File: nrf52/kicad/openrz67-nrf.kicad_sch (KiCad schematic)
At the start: 14 parts, among them J1 Camera, J2 SWD, Q1 AO3401A, SW1 B3U-1000P, U1 E73-2G4M08S1F, U2 TLP172AM, U3 TLP172AM

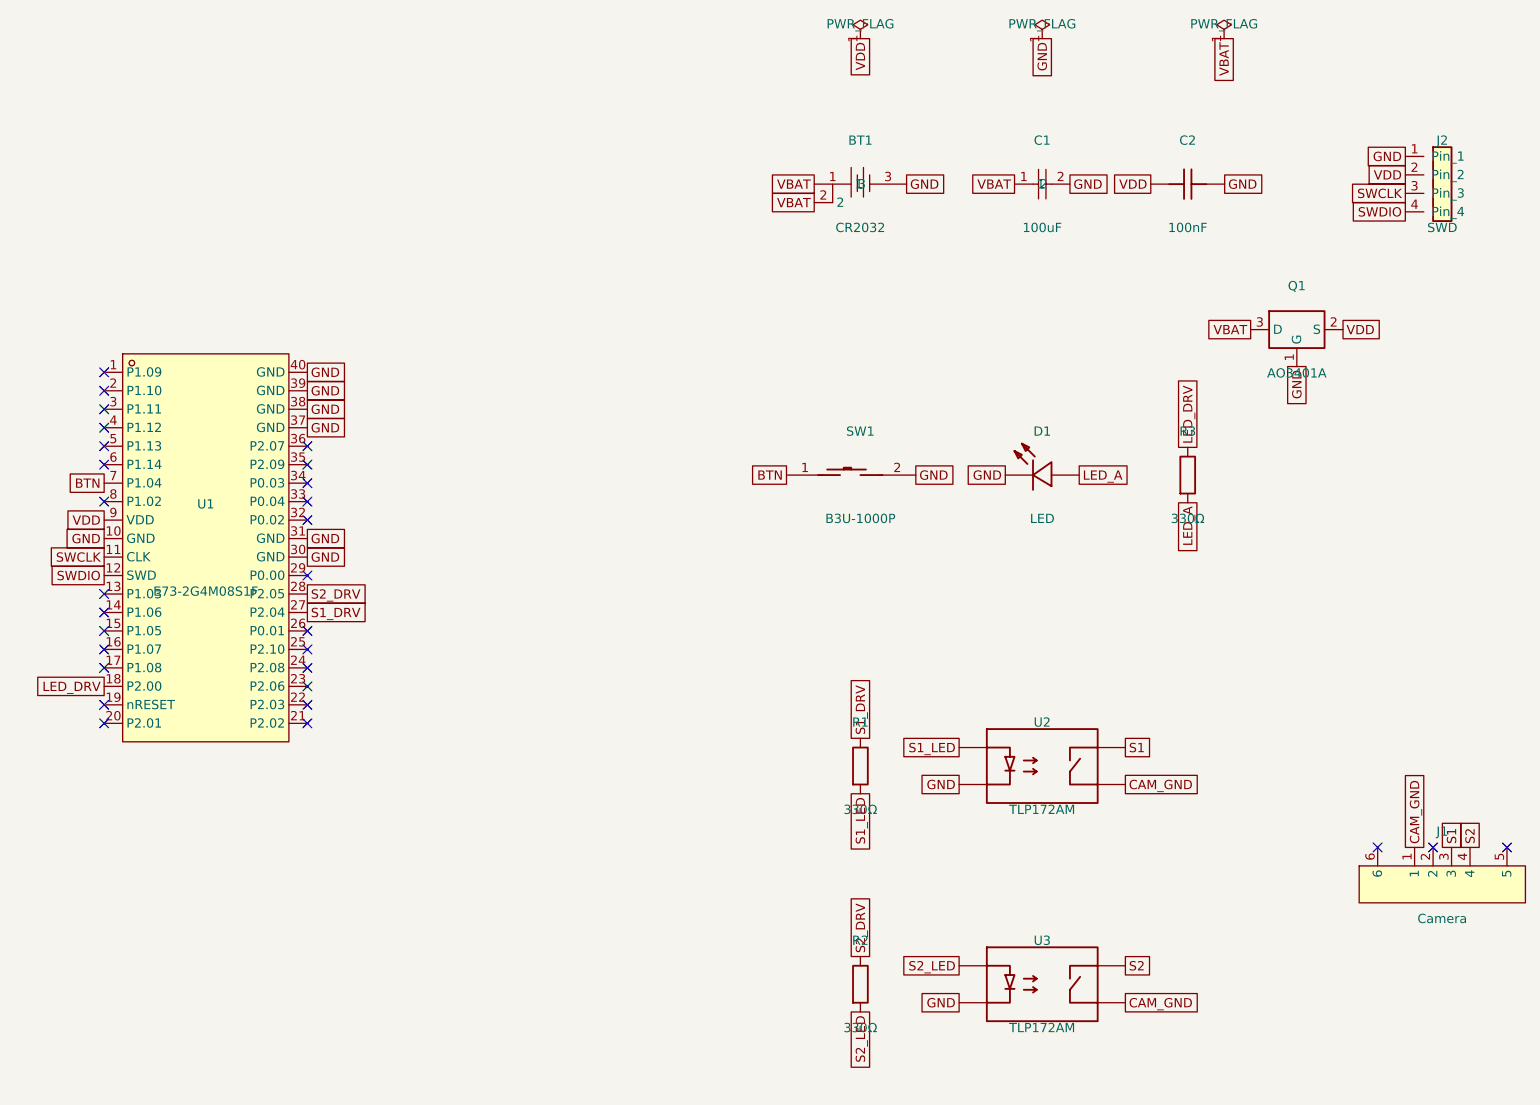
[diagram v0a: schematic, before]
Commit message: nrf52 pcb: 220 Ω relay drive, C3 at the module
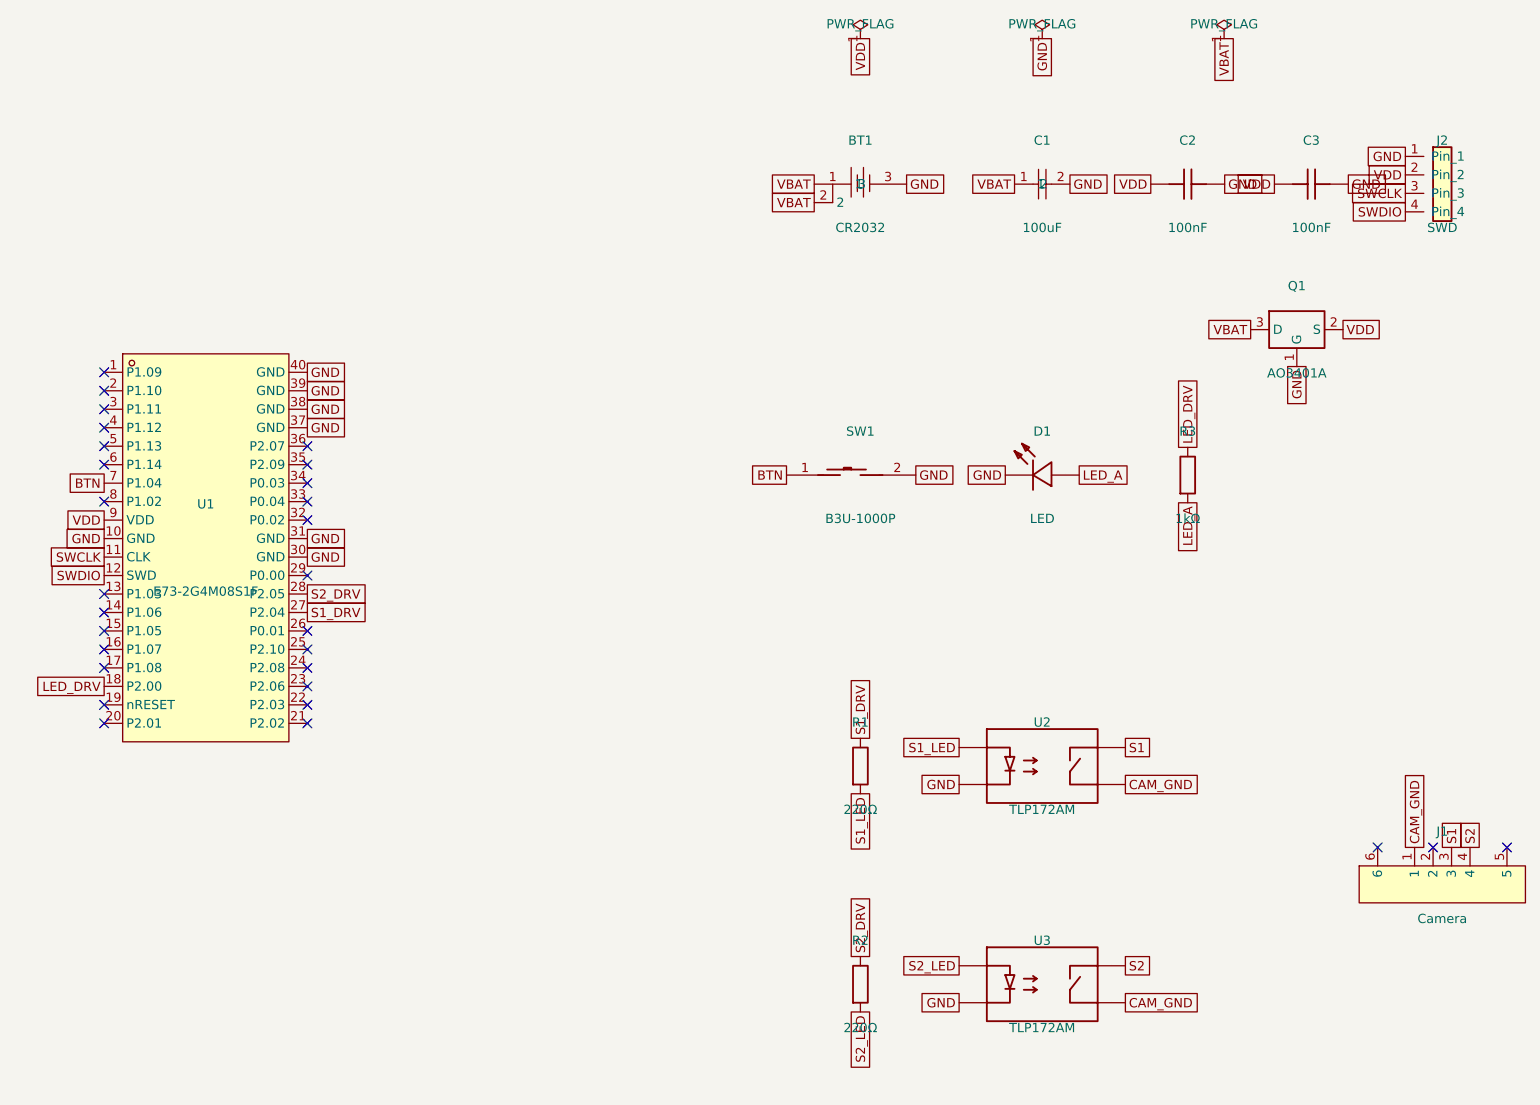
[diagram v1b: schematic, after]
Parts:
- added C3: 100nF, openrz67-nrf:C0402, symbol openrz67-nrf:GRM155R71H104KE14D
- R1, R2: value 330Ω -> 220Ω; LCSC C25104 -> C25091; MPN 0402WGF3300TCE -> 0402WGF2200TCE
- R3: value 330Ω -> 1kΩ; LCSC C25104 -> C11702; MPN 0402WGF3300TCE -> 0402WGF1001TCE
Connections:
- net GND: now also C3.2
- net VDD: now also C3.1
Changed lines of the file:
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@@
       (effects (font (size 1.27 1.27)))
     )
-    (property "Value" "330Ω" (at 150 126 0)
+    (property "Value" "220Ω" (at 150 126 0)
       (effects (font (size 1.27 1.27)))
     )
@@
       (effects (font (size 1.27 1.27)) hide)
     )
-    (property "Description" "S1 LED series, 5 mA at 3.0 V" (at 150 120 0)
-      (effects (font (size 1.27 1.27)) hide)
-    )
-    (property "LCSC" "C25104" (at 150 120 0)
-      (effects (font (size 1.27 1.27)) hide)
-    )
-    (property "MPN" "0402WGF3300TCE" (at 150 120 0)
+    (property "Description" "S1 LED series, 4 mA at 2.7 V" (at 150 120 0)
+      (effects (font (size 1.27 1.27)) hide)
+    )
+    (property "LCSC" "C25091" (at 150 120 0)
+      (effects (font (size 1.27 1.27)) hide)
+    )
+    (property "MPN" "0402WGF2200TCE" (at 150 120 0)
       (effects (font (size 1.27 1.27)) hide)
     )
@@
       (effects (font (size 1.27 1.27)))
     )
-    (property "Value" "330Ω" (at 150 156 0)
+    (property "Value" "220Ω" (at 150 156 0)
       (effects (font (size 1.27 1.27)))
     )
@@
       (effects (font (size 1.27 1.27)) hide)
     )
-    (property "LCSC" "C25104" (at 150 150 0)
-      (effects (font (size 1.27 1.27)) hide)
-    )
-    (property "MPN" "0402WGF3300TCE" (at 150 150 0)
+    (property "LCSC" "C25091" (at 150 150 0)
+      (effects (font (size 1.27 1.27)) hide)
+    )
+    (property "MPN" "0402WGF2200TCE" (at 150 150 0)
       (effects (font (size 1.27 1.27)) hide)
     )
@@
       (effects (font (size 1.27 1.27)))
     )
-    (property "Value" "330Ω" (at 195 86 0)
+    (property "Value" "1kΩ" (at 195 86 0)
       (effects (font (size 1.27 1.27)))
     )
@@
       (effects (font (size 1.27 1.27)) hide)
     )
-    (property "Description" "status LED series, same part as R1/R2" (at 195 80 0)
-      (effects (font (size 1.27 1.27)) hide)
-    )
-    (property "LCSC" "C25104" (at 195 80 0)
-      (effects (font (size 1.27 1.27)) hide)
-    )
-    (property "MPN" "0402WGF3300TCE" (at 195 80 0)
+    (property "Description" "status LED series, about 1 mA: it shares the GPIO budget with R1/R2" (at 195 80 0)
+      (effects (font (size 1.27 1.27)) hide)
+    )
+    (property "LCSC" "C11702" (at 195 80 0)
+      (effects (font (size 1.27 1.27)) hide)
+    )
+    (property "MPN" "0402WGF1001TCE" (at 195 80 0)
       (effects (font (size 1.27 1.27)) hide)
     )
@@
       (effects (font (size 1.27 1.27)) hide)
     )
-    (property "Description" "VDD decoupling at the module" (at 195 40 0)
+    (property "Description" "VDD decoupling at Q1 and the SWD connector" (at 195 40 0)
       (effects (font (size 1.27 1.27)) hide)
     )
@@
     (instances
       (project "openrz67-nrf" (path "/5d1c1d2e-0a3b-4c4d-9e5f-6a7b8c9d0e1f" (reference "C2") (unit 1)))
+    )
+  )
+  (symbol (lib_id "openrz67-nrf:GRM155R71H104KE14D") (at 212 40 0) (unit 1)
+    (in_bom yes) (on_board yes) (dnp no)
+    (property "Reference" "C3" (at 212 34 0)
+      (effects (font (size 1.27 1.27)))
+    )
+    (property "Value" "100nF" (at 212 46 0)
+      (effects (font (size 1.27 1.27)))
+    )
+    (property "Footprint" "openrz67-nrf:C0402" (at 212 40 0)
+      (effects (font (size 1.27 1.27)) hide)
+    )
+    (property "Datasheet" "" (at 212 40 0)
+      (effects (font (size 1.27 1.27)) hide)
+    )
+    (property "Description" "VDD decoupling at module pad 9, GND straight to pad 10" (at 212 40 0)
+      (effects (font (size 1.27 1.27)) hide)
+    )
+    (property "LCSC" "C1525" (at 212 40 0)
+      (effects (font (size 1.27 1.27)) hide)
+    )
+    (property "MPN" "CL05B104KO5NNNC" (at 212 40 0)
+      (effects (font (size 1.27 1.27)) hide)
+    )
+    (property "Manufacturer" "Samsung" (at 212 40 0)
+      (effects (font (size 1.27 1.27)) hide)
+    )
+    (pin "1")
+    (pin "2")
+    (instances
+      (project "openrz67-nrf" (path "/5d1c1d2e-0a3b-4c4d-9e5f-6a7b8c9d0e1f" (reference "C3") (unit 1)))
     )
   )
@@
     (effects (font (size 1.27 1.27)) (justify left))
   )
+  (global_label "VDD" (shape passive) (at 206.92 40.0 180) (fields_autoplaced yes)
+    (effects (font (size 1.27 1.27)) (justify right))
+  )
+  (global_label "GND" (shape passive) (at 217.08 40.0 0) (fields_autoplaced yes)
+    (effects (font (size 1.27 1.27)) (justify left))
+  )
